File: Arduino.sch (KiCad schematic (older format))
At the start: 0 parts

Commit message: Understanding the Arduino Module
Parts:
- added R? (x13): R, symbol R
- added SHIELD?: ARDUINO_SHIELD, symbol ARDUINO_SHIELD
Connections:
- net MISO: now also R?.2
- net MOSI: now also R?.2
- net SCLK: now also R?.2
- new net: R?.1, SHIELD?.0
- new net: R?.1, SHIELD?.1
- new net: R?.1, SHIELD?.10 ((CS_N)_10)
- new net: R?.1, SHIELD?.11 ((MOSI)_11)
- new net: R?.1, SHIELD?.12 ((MISO)_12)
- new net: R?.1, SHIELD?.13 ((SCK)_13)
- new net: R?.1, SHIELD?.8
- new net: R?.1, SHIELD?.9 ((PWM0)_9)
- new net: R?.2, SHIELD?.AD0
- new net: R?.2, SHIELD?.AD1
- new net: R?.2, SHIELD?.AD2
- new net: R?.2, SHIELD?.AD3
- new net ADC_CS_N: R?.2
- new net CURR_MEAS: R?.1
- new net DAC_CS_N: R?.2
- new net FAN_EN_N: R?.2
- new net GND: R?.1
- new net LED_EN_PWM: R?.2
- new net RELAY+: R?.2
- new net RELAY-: R?.2
- new net TACH_MEAS: R?.1
- new net V+_ADJ_MON: R?.1
- new net V-_ADJ_MON: R?.1

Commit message: Revisting the Current/Fan Module
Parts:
- added R? (x2): R, symbol R
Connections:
- net at SHIELD?.0: now also R?.1; no longer R?.1
- net at SHIELD?.10 ((CS_N)_10): now also R?.1; no longer R?.1
- net at SHIELD?.7: now also R?.1
- net at SHIELD?.V_IN: now also R?.2
- net FAN_EN_N renamed FAN_PWM
- new net +12P: R?.1
- new net FAN_MODE: R?.2
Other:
- moved on the sheet: R?
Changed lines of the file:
@@
 Text HLabel 7600 4850 2    60   Output ~ 0
 RELAY+
-Text HLabel 7600 5250 2    60   Input ~ 0
+Text HLabel 8750 4850 0    60   Input ~ 0
 RELAY-
 Text HLabel 7600 3750 2    60   Output ~ 0
@@
 Text HLabel 7600 3550 2    60   Output ~ 0
 SCLK
-Text HLabel 7600 3850 2    60   Output ~ 0
+Text HLabel 7600 4250 2    60   Output ~ 0
 DAC_CS_N
 Text HLabel 7600 3950 2    60   Output ~ 0
 LED_EN_PWM
-Text HLabel 7600 4950 2    60   Output ~ 0
-FAN_EN_N
+Text HLabel 7600 3850 2    60   Output ~ 0
+FAN_PWM
 Text HLabel 3350 4650 0    60   Input ~ 0
 CURR_MEAS
@@
 L R R?
 U 1 1 52F48765
-P 7050 4950
-F 0 "R?" V 7050 5050 40  0000 C CNN
-F 1 "R" V 7057 4951 40  0000 C CNN
-F 2 "" V 6980 4950 30  0000 C CNN
-F 3 "" H 7050 4950 30  0000 C CNN
-	1    7050 4950
-	0    -1   -1   0
-$EndComp
-Wire Wire Line
-	6450 4950 6800 4950
-Wire Wire Line
-	7300 4950 7600 4950
+P 7050 3850
+F 0 "R?" V 7050 3950 40  0000 C CNN
+F 1 "R" V 7057 3851 40  0000 C CNN
+F 2 "" V 6980 3850 30  0000 C CNN
+F 3 "" H 7050 3850 30  0000 C CNN
+	1    7050 3850
+	0    -1   -1   0
+$EndComp
+Wire Wire Line
+	6450 3850 6800 3850
+Wire Wire Line
+	7300 3850 7600 3850
 $Comp
 L R R?
@@
 	7300 4850 7600 4850
 Wire Wire Line
-	7300 5250 7600 5250
+	9050 4850 8750 4850
 $Comp
 L GND #PWR?
 U 1 1 52F49373
-P 6650 5550
-F 0 "#PWR?" H 6650 5550 30  0001 C CNN
-F 1 "GND" H 6650 5480 30  0001 C CNN
-F 2 "" H 6650 5550 60  0000 C CNN
-F 3 "" H 6650 5550 60  0000 C CNN
-	1    6650 5550
-	1    0    0    -1
+P 9700 5150
+F 0 "#PWR?" H 9700 5150 30  0001 C CNN
+F 1 "GND" H 9700 5080 30  0001 C CNN
+F 2 "" H 9700 5150 60  0000 C CNN
+F 3 "" H 9700 5150 60  0000 C CNN
+	1    9700 5150
+	-1   0    0    -1
 $EndComp
 $Comp
@@
 L R R?
 U 1 1 52F49444
-P 7050 3850
-F 0 "R?" V 7050 3950 40  0000 C CNN
-F 1 "R" V 7057 3851 40  0000 C CNN
-F 2 "" V 6980 3850 30  0000 C CNN
-F 3 "" H 7050 3850 30  0000 C CNN
-	1    7050 3850
+P 7050 4250
+F 0 "R?" V 7050 4350 40  0000 C CNN
+F 1 "R" V 7057 4251 40  0000 C CNN
+F 2 "" V 6980 4250 30  0000 C CNN
+F 3 "" H 7050 4250 30  0000 C CNN
+	1    7050 4250
 	0    -1   -1   0
 $EndComp
@@
 	7600 3750 7300 3750
 Wire Wire Line
-	7600 3850 7300 3850
-Wire Wire Line
-	6800 3850 6450 3850
+	7600 4250 7300 4250
+Wire Wire Line
+	6800 4250 6450 4250
 Wire Wire Line
 	6800 3750 6450 3750
@@
 L R R?
 U 1 1 52F49526
-P 7050 5250
-F 0 "R?" V 7050 5350 40  0000 C CNN
-F 1 "R" V 7057 5251 40  0000 C CNN
-F 2 "" V 6980 5250 30  0000 C CNN
-F 3 "" H 7050 5250 30  0000 C CNN
-	1    7050 5250
-	0    -1   -1   0
-$EndComp
-Wire Wire Line
-	6800 5250 6650 5250
-Wire Wire Line
-	6650 5250 6650 5550
+P 9300 4850
+F 0 "R?" V 9300 4950 40  0000 C CNN
+F 1 "R" V 9307 4851 40  0000 C CNN
+F 2 "" V 9230 4850 30  0000 C CNN
+F 3 "" H 9300 4850 30  0000 C CNN
+	1    9300 4850
+	0    1    -1   0
+$EndComp
+Wire Wire Line
+	9550 4850 9700 4850
+Wire Wire Line
+	9700 4850 9700 5150
 $Comp
 L R R?
@@
 Wire Wire Line
 	7600 4050 7300 4050
+Text HLabel 7600 4950 2    60   Output ~ 0
+FAN_MODE
+$Comp
+L R R?
+U 1 1 52F86CE8
+P 7050 4950
+F 0 "R?" V 7050 5050 40  0000 C CNN
+F 1 "R" V 7057 4951 40  0000 C CNN
+F 2 "" V 6980 4950 30  0000 C CNN
+F 3 "" H 7050 4950 30  0000 C CNN
+	1    7050 4950
+	0    -1   -1   0
+$EndComp
+Wire Wire Line
+	6800 4950 6450 4950
+Wire Wire Line
+	7300 4950 7600 4950
+$Comp
+L R R?
+U 1 1 52F870EF
+P 4000 4250
+F 0 "R?" V 4000 4350 40  0000 C CNN
+F 1 "R" V 4007 4251 40  0000 C CNN
+F 2 "" V 3930 4250 30  0000 C CNN
+F 3 "" H 4000 4250 30  0000 C CNN
+	1    4000 4250
+	0    -1   -1   0
+$EndComp
+Wire Wire Line
+	4250 4250 4550 4250
+Wire Wire Line
+	3750 4250 3500 4250
+Wire Wire Line
+	3500 4250 3500 3900
+$Comp
+L +12P #PWR?
+U 1 1 52F8713D
+P 3500 3900
+F 0 "#PWR?" H 3500 3870 30  0001 C CNN
+F 1 "+12P" H 3500 4000 30  0000 C CNN
+F 2 "" H 3500 3900 60  0000 C CNN
+F 3 "" H 3500 3900 60  0000 C CNN
+	1    3500 3900
+	1    0    0    -1
+$EndComp
 $EndSCHEMATC

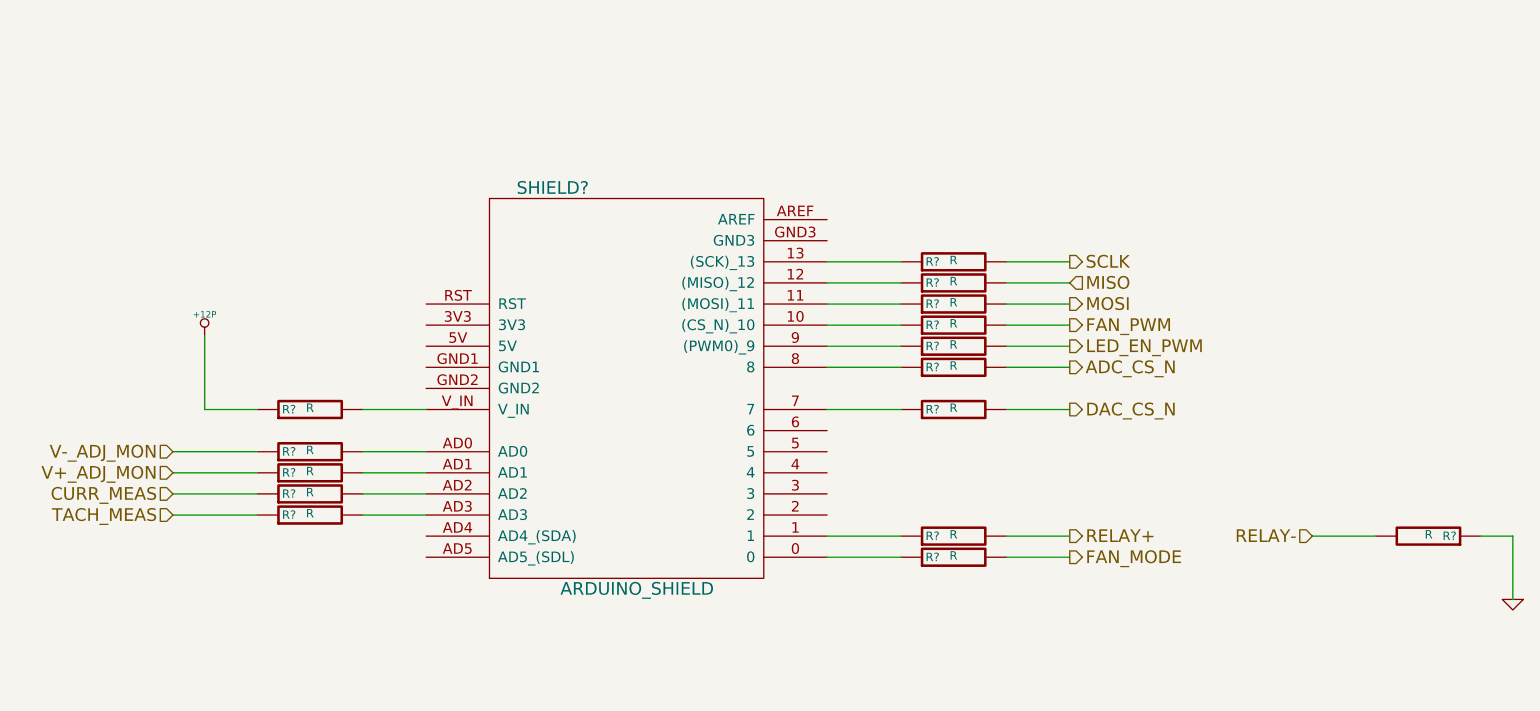
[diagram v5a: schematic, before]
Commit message: Associating and Placing the Relay Module
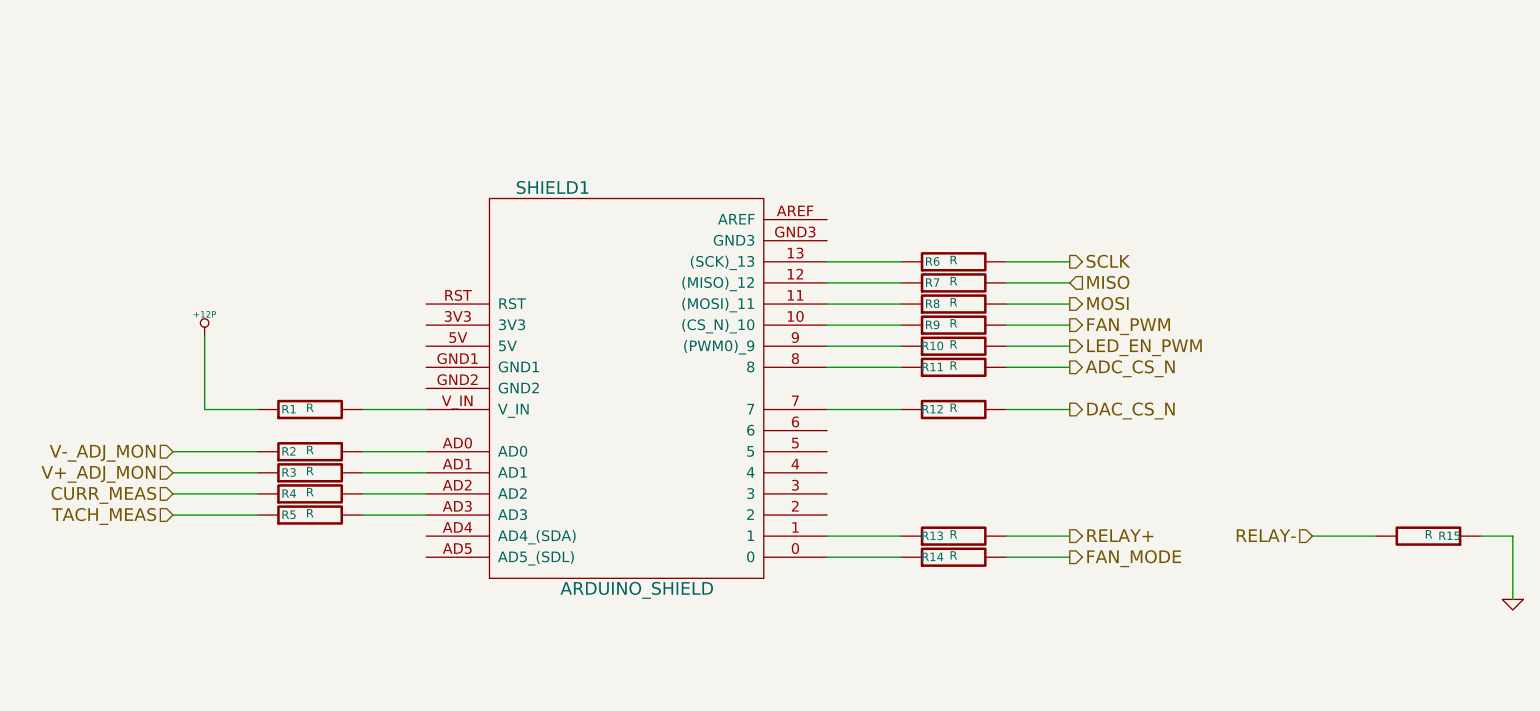
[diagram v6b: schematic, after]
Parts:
- gave numbers to parts that had none: 16
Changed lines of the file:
@@
 CURR_MEAS
 $Comp
-L ARDUINO_SHIELD SHIELD?
+L ARDUINO_SHIELD SHIELD1
 U 1 1 52F47B3E
 P 5500 4150
-F 0 "SHIELD?" H 5150 5100 60  0000 C CNN
+F 0 "SHIELD1" H 5150 5100 60  0000 C CNN
 F 1 "ARDUINO_SHIELD" H 5550 3200 60  0000 C CNN
 F 2 "" H 5500 4150 60  0000 C CNN
@@
 TACH_MEAS
 $Comp
-L R R?
+L R R9
 U 1 1 52F48765
 P 7050 3850
-F 0 "R?" V 7050 3950 40  0000 C CNN
+F 0 "R9" V 7050 3950 40  0000 C CNN
 F 1 "R" V 7057 3851 40  0000 C CNN
 F 2 "" V 6980 3850 30  0000 C CNN
@@
 	7300 3850 7600 3850
 $Comp
-L R R?
+L R R13
 U 1 1 52F48790
 P 7050 4850
-F 0 "R?" V 7050 4950 40  0000 C CNN
+F 0 "R13" V 7050 4950 40  0000 C CNN
 F 1 "R" V 7057 4851 40  0000 C CNN
 F 2 "" V 6980 4850 30  0000 C CNN
@@
 	9050 4850 8750 4850
 $Comp
-L GND #PWR?
+L GND #PWR01
 U 1 1 52F49373
 P 9700 5150
-F 0 "#PWR?" H 9700 5150 30  0001 C CNN
+F 0 "#PWR01" H 9700 5150 30  0001 C CNN
 F 1 "GND" H 9700 5080 30  0001 C CNN
 F 2 "" H 9700 5150 60  0000 C CNN
@@
 $EndComp
 $Comp
-L R R?
+L R R5
 U 1 1 52F49385
 P 4000 4750
-F 0 "R?" V 4000 4850 40  0000 C CNN
+F 0 "R5" V 4000 4850 40  0000 C CNN
 F 1 "R" V 4007 4751 40  0000 C CNN
 F 2 "" V 3930 4750 30  0000 C CNN
@@
 $EndComp
 $Comp
-L R R?
+L R R4
 U 1 1 52F49390
 P 4000 4650
-F 0 "R?" V 4000 4750 40  0000 C CNN
+F 0 "R4" V 4000 4750 40  0000 C CNN
 F 1 "R" V 4007 4651 40  0000 C CNN
 F 2 "" V 3930 4650 30  0000 C CNN
@@
 V-_ADJ_MON
 $Comp
-L R R?
+L R R3
 U 1 1 52F493D3
 P 4000 4550
-F 0 "R?" V 4000 4650 40  0000 C CNN
+F 0 "R3" V 4000 4650 40  0000 C CNN
 F 1 "R" V 4007 4551 40  0000 C CNN
 F 2 "" V 3930 4550 30  0000 C CNN
@@
 $EndComp
 $Comp
-L R R?
+L R R2
 U 1 1 52F493DE
 P 4000 4450
-F 0 "R?" V 4000 4550 40  0000 C CNN
+F 0 "R2" V 4000 4550 40  0000 C CNN
 F 1 "R" V 4007 4451 40  0000 C CNN
 F 2 "" V 3930 4450 30  0000 C CNN
@@
 	3750 4550 3350 4550
 $Comp
-L R R?
+L R R12
 U 1 1 52F49444
 P 7050 4250
-F 0 "R?" V 7050 4350 40  0000 C CNN
+F 0 "R12" V 7050 4350 40  0000 C CNN
 F 1 "R" V 7057 4251 40  0000 C CNN
 F 2 "" V 6980 4250 30  0000 C CNN
@@
 $EndComp
 $Comp
-L R R?
+L R R8
 U 1 1 52F4944F
 P 7050 3750
-F 0 "R?" V 7050 3850 40  0000 C CNN
+F 0 "R8" V 7050 3850 40  0000 C CNN
 F 1 "R" V 7057 3751 40  0000 C CNN
 F 2 "" V 6980 3750 30  0000 C CNN
@@
 $EndComp
 $Comp
-L R R?
+L R R7
 U 1 1 52F49464
 P 7050 3650
-F 0 "R?" V 7050 3750 40  0000 C CNN
+F 0 "R7" V 7050 3750 40  0000 C CNN
 F 1 "R" V 7057 3651 40  0000 C CNN
 F 2 "" V 6980 3650 30  0000 C CNN
@@
 $EndComp
 $Comp
-L R R?
+L R R6
 U 1 1 52F4946F
 P 7050 3550
-F 0 "R?" V 7050 3650 40  0000 C CNN
+F 0 "R6" V 7050 3650 40  0000 C CNN
 F 1 "R" V 7057 3551 40  0000 C CNN
 F 2 "" V 6980 3550 30  0000 C CNN
@@
 	6800 3550 6450 3550
 $Comp
-L R R?
+L R R15
 U 1 1 52F49526
 P 9300 4850
-F 0 "R?" V 9300 4950 40  0000 C CNN
+F 0 "R15" V 9300 4950 40  0000 C CNN
 F 1 "R" V 9307 4851 40  0000 C CNN
 F 2 "" V 9230 4850 30  0000 C CNN
@@
 	9700 4850 9700 5150
 $Comp
-L R R?
+L R R10
 U 1 1 52F4956B
 P 7050 3950
-F 0 "R?" V 7050 4050 40  0000 C CNN
+F 0 "R10" V 7050 4050 40  0000 C CNN
 F 1 "R" V 7057 3951 40  0000 C CNN
 F 2 "" V 6980 3950 30  0000 C CNN
@@
 	6800 3950 6450 3950
 $Comp
-L R R?
+L R R11
 U 1 1 52F4E7B6
 P 7050 4050
-F 0 "R?" V 7050 4150 40  0000 C CNN
+F 0 "R11" V 7050 4150 40  0000 C CNN
 F 1 "R" V 7057 4051 40  0000 C CNN
 F 2 "" V 6980 4050 30  0000 C CNN
@@
 FAN_MODE
 $Comp
-L R R?
+L R R14
 U 1 1 52F86CE8
 P 7050 4950
-F 0 "R?" V 7050 5050 40  0000 C CNN
+F 0 "R14" V 7050 5050 40  0000 C CNN
 F 1 "R" V 7057 4951 40  0000 C CNN
 F 2 "" V 6980 4950 30  0000 C CNN
@@
 	7300 4950 7600 4950
 $Comp
-L R R?
+L R R1
 U 1 1 52F870EF
 P 4000 4250
-F 0 "R?" V 4000 4350 40  0000 C CNN
+F 0 "R1" V 4000 4350 40  0000 C CNN
 F 1 "R" V 4007 4251 40  0000 C CNN
 F 2 "" V 3930 4250 30  0000 C CNN
@@
 	3500 4250 3500 3900
 $Comp
-L +12P #PWR?
+L +12P #PWR02
 U 1 1 52F8713D
 P 3500 3900
-F 0 "#PWR?" H 3500 3870 30  0001 C CNN
+F 0 "#PWR02" H 3500 3870 30  0001 C CNN
 F 1 "+12P" H 3500 4000 30  0000 C CNN
 F 2 "" H 3500 3900 60  0000 C CNN

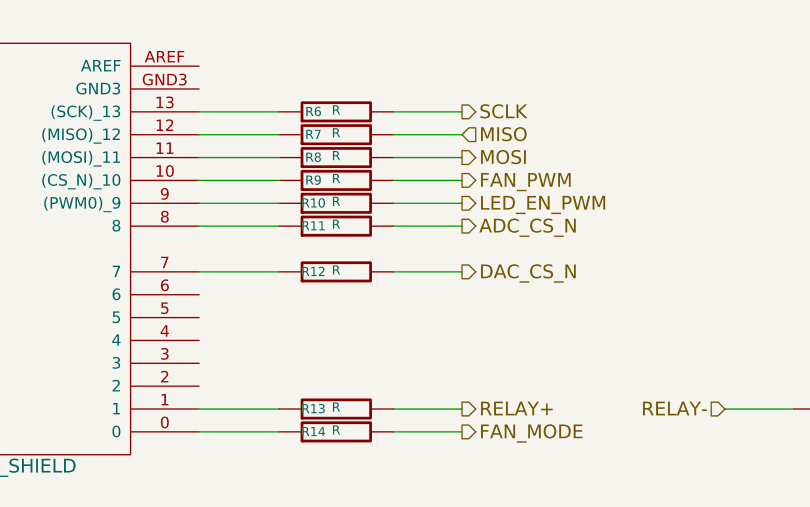
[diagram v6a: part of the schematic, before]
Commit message: Associating and Placing the Thermocouple Module
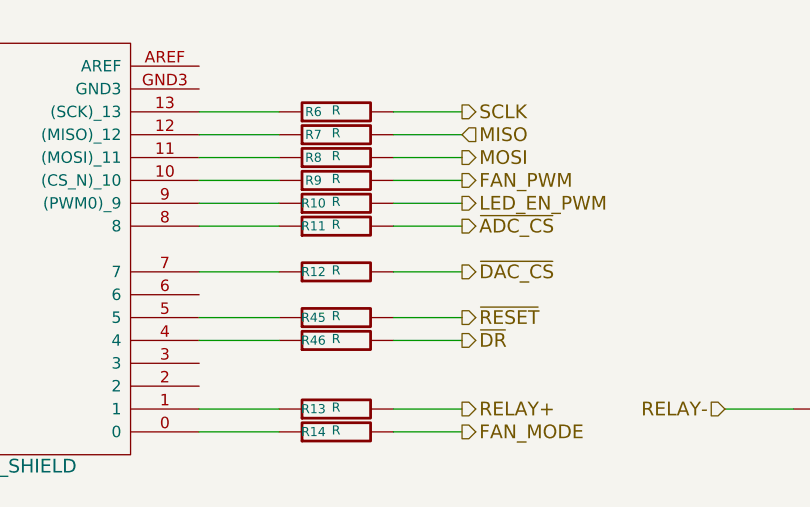
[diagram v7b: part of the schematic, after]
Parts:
- added R45, R46: R, symbol R
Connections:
- net at SHIELD1.4: now also R46.1
- net at SHIELD1.5: now also R45.1
- net ADC_CS_N renamed ~ADC_CS
- net DAC_CS_N renamed ~DAC_CS
- new net ~DR: R46.2
- new net ~RESET: R45.2
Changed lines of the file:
@@
 LIBS:MyComponents
 LIBS:arduino_shieldsNCL
+LIBS:BenchBudEE
 LIBS:BenchBuddy-cache
 EELAYER 24 0
@@
 SCLK
 Text HLabel 7600 4250 2    60   Output ~ 0
-DAC_CS_N
+~DAC_CS
 Text HLabel 7600 3950 2    60   Output ~ 0
 LED_EN_PWM
@@
 	6800 4050 6450 4050
 Text HLabel 7600 4050 2    60   Output ~ 0
-ADC_CS_N
+~ADC_CS
 Wire Wire Line
 	7600 4050 7300 4050
@@
 	1    0    0    -1
 $EndComp
+Text HLabel 7600 4450 2    60   Output ~ 0
+~RESET
+$Comp
+L R R45
+U 1 1 5304E3AE
+P 7050 4450
+F 0 "R45" V 7050 4550 40  0000 C CNN
+F 1 "R" V 7057 4451 40  0000 C CNN
+F 2 "" V 6980 4450 30  0000 C CNN
+F 3 "" H 7050 4450 30  0000 C CNN
+	1    7050 4450
+	0    -1   -1   0
+$EndComp
+Wire Wire Line
+	7600 4450 7300 4450
+Wire Wire Line
+	6800 4450 6450 4450
+Text HLabel 7600 4550 2    60   Output ~ 0
+~DR
+$Comp
+L R R46
+U 1 1 5304E3B7
+P 7050 4550
+F 0 "R46" V 7050 4650 40  0000 C CNN
+F 1 "R" V 7057 4551 40  0000 C CNN
+F 2 "" V 6980 4550 30  0000 C CNN
+F 3 "" H 7050 4550 30  0000 C CNN
+	1    7050 4550
+	0    -1   -1   0
+$EndComp
+Wire Wire Line
+	7600 4550 7300 4550
+Wire Wire Line
+	6800 4550 6450 4550
 $EndSCHEMATC

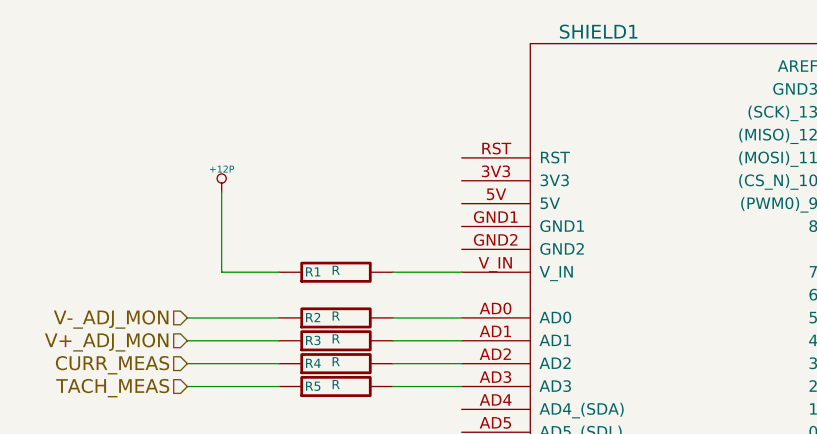
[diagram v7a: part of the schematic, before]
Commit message: Associating and Placing the Arduino Module
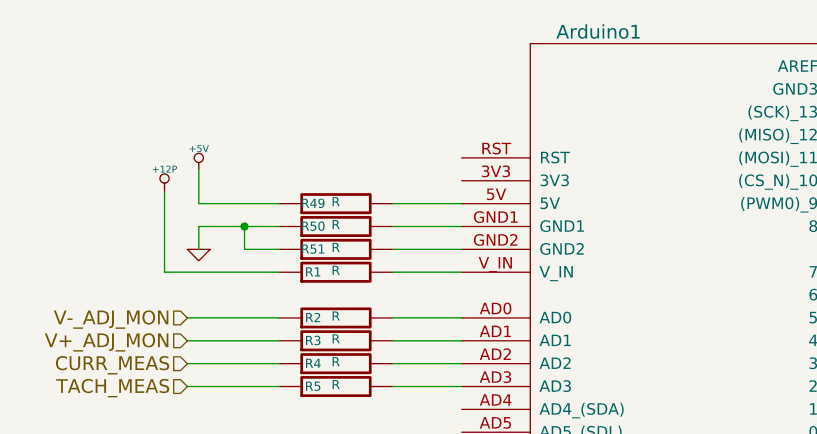
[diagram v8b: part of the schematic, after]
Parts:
- added R49, R50, R51: R, symbol R
- renumbered SHIELD1 to Arduino1
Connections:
- net GND: now also R50.1, R51.1
- net at Arduino1.5V: now also R49.2
- net at Arduino1.GND1: now also R50.2
- net at Arduino1.GND2: now also R51.2
- new net +5V: R49.1
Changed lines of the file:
@@
 CURR_MEAS
 $Comp
-L ARDUINO_SHIELD SHIELD1
+L ARDUINO_SHIELD Arduino1
 U 1 1 52F47B3E
 P 5500 4150
-F 0 "SHIELD1" H 5150 5100 60  0000 C CNN
+F 0 "Arduino1" H 5150 5100 60  0000 C CNN
 F 1 "ARDUINO_SHIELD" H 5550 3200 60  0000 C CNN
 F 2 "" H 5500 4150 60  0000 C CNN
@@
 Wire Wire Line
 	4250 4250 4550 4250
-Wire Wire Line
-	3750 4250 3500 4250
-Wire Wire Line
-	3500 4250 3500 3900
 $Comp
 L +12P #PWR02
 U 1 1 52F8713D
-P 3500 3900
-F 0 "#PWR02" H 3500 3870 30  0001 C CNN
-F 1 "+12P" H 3500 4000 30  0000 C CNN
-F 2 "" H 3500 3900 60  0000 C CNN
-F 3 "" H 3500 3900 60  0000 C CNN
-	1    3500 3900
+P 3250 3900
+F 0 "#PWR02" H 3250 3870 30  0001 C CNN
+F 1 "+12P" H 3250 4000 30  0000 C CNN
+F 2 "" H 3250 3900 60  0000 C CNN
+F 3 "" H 3250 3900 60  0000 C CNN
+	1    3250 3900
 	1    0    0    -1
 $EndComp
@@
 Wire Wire Line
 	6800 4550 6450 4550
+$Comp
+L R R51
+U 1 1 5306C012
+P 4000 4150
+F 0 "R51" V 4000 4250 40  0000 C CNN
+F 1 "R" V 4007 4151 40  0000 C CNN
+F 2 "" V 3930 4150 30  0000 C CNN
+F 3 "" H 4000 4150 30  0000 C CNN
+	1    4000 4150
+	0    -1   -1   0
+$EndComp
+$Comp
+L R R50
+U 1 1 5306C01D
+P 4000 4050
+F 0 "R50" V 4000 4150 40  0000 C CNN
+F 1 "R" V 4007 4051 40  0000 C CNN
+F 2 "" V 3930 4050 30  0000 C CNN
+F 3 "" H 4000 4050 30  0000 C CNN
+	1    4000 4050
+	0    -1   -1   0
+$EndComp
+$Comp
+L R R49
+U 1 1 5306C028
+P 4000 3950
+F 0 "R49" V 4000 4050 40  0000 C CNN
+F 1 "R" V 4007 3951 40  0000 C CNN
+F 2 "" V 3930 3950 30  0000 C CNN
+F 3 "" H 4000 3950 30  0000 C CNN
+	1    4000 3950
+	0    -1   -1   0
+$EndComp
+Wire Wire Line
+	4550 3950 4250 3950
+Wire Wire Line
+	4550 4050 4250 4050
+Wire Wire Line
+	4550 4150 4250 4150
+Wire Wire Line
+	3750 4250 3250 4250
+Wire Wire Line
+	3250 4250 3250 3900
+$Comp
+L GND #PWR03
+U 1 1 5306C13A
+P 3400 4150
+F 0 "#PWR03" H 3400 4150 30  0001 C CNN
+F 1 "GND" H 3400 4080 30  0001 C CNN
+F 2 "" H 3400 4150 60  0000 C CNN
+F 3 "" H 3400 4150 60  0000 C CNN
+	1    3400 4150
+	-1   0    0    -1
+$EndComp
+Wire Wire Line
+	3750 4050 3400 4050
+Wire Wire Line
+	3400 4050 3400 4150
+Wire Wire Line
+	3750 4150 3600 4150
+Wire Wire Line
+	3600 4150 3600 4050
+Connection ~ 3600 4050
+$Comp
+L +5V #PWR04
+U 1 1 5306C1AA
+P 3400 3800
+F 0 "#PWR04" H 3400 3890 20  0001 C CNN
+F 1 "+5V" H 3400 3890 30  0000 C CNN
+F 2 "" H 3400 3800 60  0000 C CNN
+F 3 "" H 3400 3800 60  0000 C CNN
+	1    3400 3800
+	1    0    0    -1
+$EndComp
+Wire Wire Line
+	3400 3800 3400 3950
+Wire Wire Line
+	3400 3950 3750 3950
 $EndSCHEMATC
